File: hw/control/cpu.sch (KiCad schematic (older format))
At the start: 18 parts, among them J301 Conn_02x05_Odd_Even, J302 Conn_01x04, J303 Raspberry_Pi_0_2_3, J304 Micro_SD_Card, J305 Conn_01x06

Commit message: [hw] Assign most of the controller footprints
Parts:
- C301, C302, C303, C304, C305: footprint (none) -> Capacitor_SMD:C_0805_2012Metric_Pad1.18x1.45mm_HandSolder
- J301: footprint (none) -> Connector_PinHeader_2.54mm:PinHeader_2x05_P2.54mm_Vertical
- J302: footprint (none) -> Connector_PinHeader_2.54mm:PinHeader_1x04_P2.54mm_Vertical
- J303: footprint (none) -> Connector_PinHeader_2.54mm:PinHeader_2x20_P2.54mm_Vertical
- J305: footprint (none) -> Connector_PinHeader_2.54mm:PinHeader_1x06_P2.54mm_Vertical
- JP301, JP302: footprint (none) -> Jumper:SolderJumper-3_P1.3mm_Bridged12_RoundedPad1.0x1.5mm_NumberLabels
- R301, R302, R303, R304, R305, R306: footprint (none) -> Resistor_SMD:R_0805_2012Metric_Pad1.20x1.40mm_HandSolder
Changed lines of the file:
@@
 F 0 "J301" H 9800 1967 50  0000 C CNN
 F 1 "Conn_02x05_Odd_Even" H 9800 1876 50  0000 C CNN
-F 2 "" H 9750 1550 50  0001 C CNN
+F 2 "Connector_PinHeader_2.54mm:PinHeader_2x05_P2.54mm_Vertical" H 9750 1550 50  0001 C CNN
 F 3 "~" H 9750 1550 50  0001 C CNN
 	1    9750 1550
@@
 F 0 "R302" V 4493 2400 50  0000 C CNN
 F 1 "33R" V 4584 2400 50  0000 C CNN
-F 2 "" V 4630 2400 50  0001 C CNN
+F 2 "Resistor_SMD:R_0805_2012Metric_Pad1.20x1.40mm_HandSolder" V 4630 2400 50  0001 C CNN
 F 3 "~" H 4700 2400 50  0001 C CNN
 	1    4700 2400
@@
 F 0 "R301" V 4493 2050 50  0000 C CNN
 F 1 "33R" V 4584 2050 50  0000 C CNN
-F 2 "" V 4630 2050 50  0001 C CNN
+F 2 "Resistor_SMD:R_0805_2012Metric_Pad1.20x1.40mm_HandSolder" V 4630 2050 50  0001 C CNN
 F 3 "~" H 4700 2050 50  0001 C CNN
 	1    4700 2050
@@
 F 0 "R304" H 1430 6554 50  0000 R CNN
 F 1 "33R" H 1430 6645 50  0000 R CNN
-F 2 "" V 1430 6600 50  0001 C CNN
+F 2 "Resistor_SMD:R_0805_2012Metric_Pad1.20x1.40mm_HandSolder" V 1430 6600 50  0001 C CNN
 F 3 "~" H 1500 6600 50  0001 C CNN
 	1    1500 6600
@@
 F 0 "R305" H 1220 6846 50  0000 L CNN
 F 1 "33R" H 1220 6755 50  0000 L CNN
-F 2 "" V 1080 6800 50  0001 C CNN
+F 2 "Resistor_SMD:R_0805_2012Metric_Pad1.20x1.40mm_HandSolder" V 1080 6800 50  0001 C CNN
 F 3 "~" H 1150 6800 50  0001 C CNN
 	1    1150 6800
@@
 F 0 "C305" H 2515 5696 50  0000 L CNN
 F 1 "100n" H 2515 5605 50  0000 L CNN
-F 2 "" H 2438 5500 50  0001 C CNN
+F 2 "Capacitor_SMD:C_0805_2012Metric_Pad1.18x1.45mm_HandSolder" H 2438 5500 50  0001 C CNN
 F 3 "~" H 2400 5650 50  0001 C CNN
 	1    2400 5650
@@
 F 0 "C302" H 1515 1246 50  0000 L CNN
 F 1 "100n" H 1515 1155 50  0000 L CNN
-F 2 "" H 1438 1050 50  0001 C CNN
+F 2 "Capacitor_SMD:C_0805_2012Metric_Pad1.18x1.45mm_HandSolder" H 1438 1050 50  0001 C CNN
 F 3 "~" H 1400 1200 50  0001 C CNN
 	1    1400 1200
@@
 F 0 "C303" H 1965 1246 50  0000 L CNN
 F 1 "100n" H 1965 1155 50  0000 L CNN
-F 2 "" H 1888 1050 50  0001 C CNN
+F 2 "Capacitor_SMD:C_0805_2012Metric_Pad1.18x1.45mm_HandSolder" H 1888 1050 50  0001 C CNN
 F 3 "~" H 1850 1200 50  0001 C CNN
 	1    1850 1200
@@
 F 0 "C304" H 2415 1246 50  0000 L CNN
 F 1 "100n" H 2415 1155 50  0000 L CNN
-F 2 "" H 2338 1050 50  0001 C CNN
+F 2 "Capacitor_SMD:C_0805_2012Metric_Pad1.18x1.45mm_HandSolder" H 2338 1050 50  0001 C CNN
 F 3 "~" H 2300 1200 50  0001 C CNN
 	1    2300 1200
@@
 F 0 "C301" H 1065 1246 50  0000 L CNN
 F 1 "100n" H 1065 1155 50  0000 L CNN
-F 2 "" H 988 1050 50  0001 C CNN
+F 2 "Capacitor_SMD:C_0805_2012Metric_Pad1.18x1.45mm_HandSolder" H 988 1050 50  0001 C CNN
 F 3 "~" H 950 1200 50  0001 C CNN
 	1    950  1200
@@
 F 0 "J303" H 6900 2250 50  0000 C CNN
 F 1 "Raspberry_Pi_0_2_3" H 7200 2350 50  0000 C CNN
-F 2 "" H 6500 3650 50  0001 C CNN
+F 2 "Connector_PinHeader_2.54mm:PinHeader_2x20_P2.54mm_Vertical" H 6500 3650 50  0001 C CNN
 F 3 "https://www.raspberrypi.org/documentation/hardware/raspberrypi/schematics/rpi_SCH_3bplus_1p0_reduced.pdf" H 6500 3650 50  0001 C CNN
 	1    6500 3650
@@
 F 0 "J302" H 3568 2517 50  0000 C CNN
 F 1 "Conn_01x04" H 3568 2426 50  0000 C CNN
-F 2 "" H 3650 2200 50  0001 C CNN
+F 2 "Connector_PinHeader_2.54mm:PinHeader_1x04_P2.54mm_Vertical" H 3650 2200 50  0001 C CNN
 F 3 "~" H 3650 2200 50  0001 C CNN
 	1    3650 2200
@@
 F 0 "R303" H 1920 6546 50  0000 L CNN
 F 1 "33R" H 1920 6455 50  0000 L CNN
-F 2 "" V 1780 6500 50  0001 C CNN
+F 2 "Resistor_SMD:R_0805_2012Metric_Pad1.20x1.40mm_HandSolder" V 1780 6500 50  0001 C CNN
 F 3 "~" H 1850 6500 50  0001 C CNN
 	1    1850 6500
@@
 F 0 "R306" H 870 7046 50  0000 L CNN
 F 1 "33R" H 870 6955 50  0000 L CNN
-F 2 "" V 730 7000 50  0001 C CNN
+F 2 "Resistor_SMD:R_0805_2012Metric_Pad1.20x1.40mm_HandSolder" V 730 7000 50  0001 C CNN
 F 3 "~" H 800 7000 50  0001 C CNN
 	1    800  7000
@@
 F 0 "J305" H 5630 6692 50  0000 L CNN
 F 1 "Conn_01x06" H 5630 6601 50  0000 L CNN
-F 2 "" H 5550 6700 50  0001 C CNN
+F 2 "Connector_PinHeader_2.54mm:PinHeader_1x06_P2.54mm_Vertical" H 5550 6700 50  0001 C CNN
 F 3 "~" H 5550 6700 50  0001 C CNN
 	1    5550 6700
@@
 F 0 "JP301" H 8300 4405 50  0000 C CNN
 F 1 "Jumper" H 8300 4314 50  0000 C CNN
-F 2 "" H 8300 4200 50  0001 C CNN
+F 2 "Jumper:SolderJumper-3_P1.3mm_Bridged12_RoundedPad1.0x1.5mm_NumberLabels" H 8300 4200 50  0001 C CNN
 F 3 "~" H 8300 4200 50  0001 C CNN
 	1    8300 4200
@@
 F 0 "JP302" H 8000 4805 50  0000 C CNN
 F 1 "Jumper" H 8000 4714 50  0000 C CNN
-F 2 "" H 8000 4600 50  0001 C CNN
+F 2 "Jumper:SolderJumper-3_P1.3mm_Bridged12_RoundedPad1.0x1.5mm_NumberLabels" H 8000 4600 50  0001 C CNN
 F 3 "~" H 8000 4600 50  0001 C CNN
 	1    8000 4600

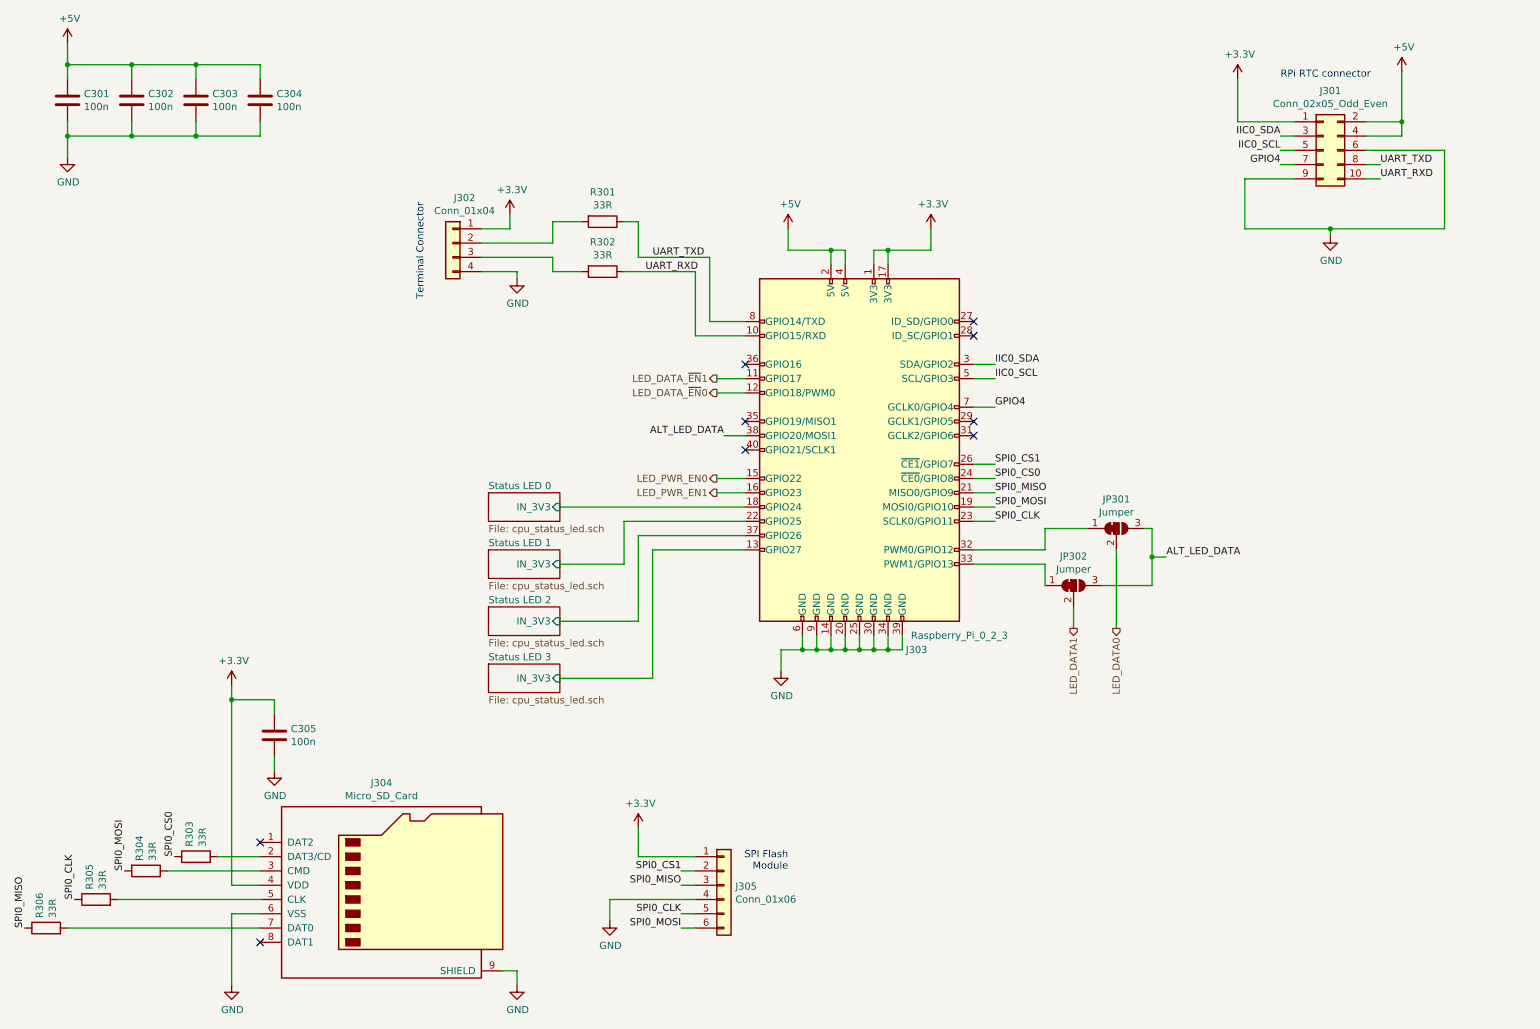
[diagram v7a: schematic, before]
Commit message: [hw] Assign control board footprints
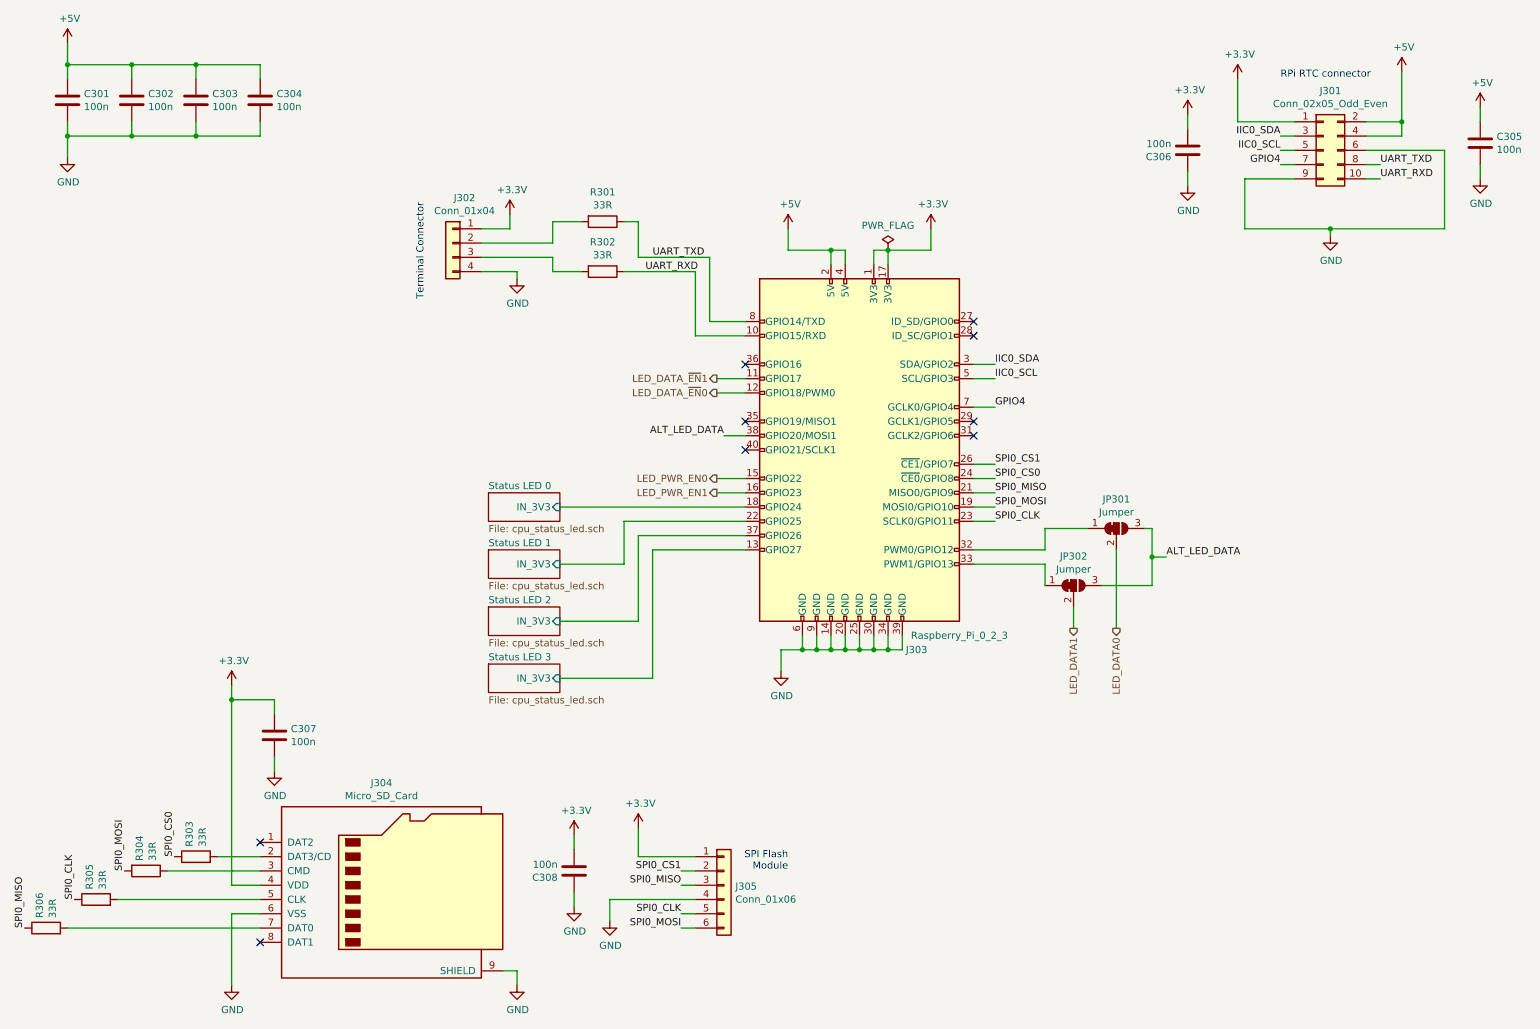
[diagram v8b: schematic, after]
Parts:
- added C305, C306, C308: 100n, Capacitor_SMD:C_0805_2012Metric_Pad1.18x1.45mm_HandSolder, symbol Device:C
- renumbered C305 to C307
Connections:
- net +3V3: now also C306.2, C308.2
- net +5V: now also C305.1
- net GND: now also C305.2, C306.1, C308.1
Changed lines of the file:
@@
 P 5950 5200
 AR Path="/614A2C71" Ref="#PWR?"  Part="1"
-AR Path="/6148E1AC/614A2C71" Ref="#PWR0310"  Part="1"
-F 0 "#PWR0310" H 5950 4950 50  0001 C CNN
+AR Path="/6148E1AC/614A2C71" Ref="#PWR0314"  Part="1"
+F 0 "#PWR0314" H 5950 4950 50  0001 C CNN
 F 1 "GND" H 5955 5027 50  0000 C CNN
 F 2 "" H 5950 5200 50  0001 C CNN
@@
 P 6000 2100
 AR Path="/614A2C87" Ref="#PWR?"  Part="1"
-AR Path="/6148E1AC/614A2C87" Ref="#PWR0306"  Part="1"
-F 0 "#PWR0306" H 6000 1950 50  0001 C CNN
+AR Path="/6148E1AC/614A2C87" Ref="#PWR0310"  Part="1"
+F 0 "#PWR0310" H 6000 1950 50  0001 C CNN
 F 1 "+5V" H 6015 2273 50  0000 C CNN
 F 2 "" H 6000 2100 50  0001 C CNN
@@
 P 7000 2100
 AR Path="/614A2C91" Ref="#PWR?"  Part="1"
-AR Path="/6148E1AC/614A2C91" Ref="#PWR0307"  Part="1"
-F 0 "#PWR0307" H 7000 1950 50  0001 C CNN
+AR Path="/6148E1AC/614A2C91" Ref="#PWR0311"  Part="1"
+F 0 "#PWR0311" H 7000 1950 50  0001 C CNN
 F 1 "+3.3V" H 7015 2273 50  0000 C CNN
 F 2 "" H 7000 2100 50  0001 C CNN
@@
 P 9800 2150
 AR Path="/614A2CB4" Ref="#PWR?"  Part="1"
-AR Path="/6148E1AC/614A2CB4" Ref="#PWR0308"  Part="1"
-F 0 "#PWR0308" H 9800 1900 50  0001 C CNN
+AR Path="/6148E1AC/614A2CB4" Ref="#PWR0312"  Part="1"
+F 0 "#PWR0312" H 9800 1900 50  0001 C CNN
 F 1 "GND" H 9805 1977 50  0000 C CNN
 F 2 "" H 9800 2150 50  0001 C CNN
@@
 	1    0    0    -1
 $EndComp
-Wire Wire Line
-	10600 2100 10600 1550
 Wire Wire Line
 	10600 1550 10050 1550
@@
 LED_PWR_EN1
 $Comp
-L power:GND #PWR0309
+L power:GND #PWR0313
 U 1 1 6146B045
 P 4100 2450
-F 0 "#PWR0309" H 4100 2200 50  0001 C CNN
+F 0 "#PWR0313" H 4100 2200 50  0001 C CNN
 F 1 "GND" H 4105 2277 50  0000 C CNN
 F 2 "" H 4100 2450 50  0001 C CNN
@@
 	7300 4050 7450 4050
 $Comp
-L power:+3.3V #PWR0311
+L power:+3.3V #PWR0315
 U 1 1 614C61E8
 P 2100 5300
-F 0 "#PWR0311" H 2100 5150 50  0001 C CNN
+F 0 "#PWR0315" H 2100 5150 50  0001 C CNN
 F 1 "+3.3V" H 2115 5473 50  0000 C CNN
 F 2 "" H 2100 5300 50  0001 C CNN
@@
 $EndComp
 $Comp
-L Device:C C305
+L Device:C C307
 U 1 1 614C7B6C
 P 2400 5650
-F 0 "C305" H 2515 5696 50  0000 L CNN
+F 0 "C307" H 2515 5696 50  0000 L CNN
 F 1 "100n" H 2515 5605 50  0000 L CNN
 F 2 "Capacitor_SMD:C_0805_2012Metric_Pad1.18x1.45mm_HandSolder" H 2438 5500 50  0001 C CNN
@@
 $EndComp
 $Comp
-L power:GND #PWR0312
+L power:GND #PWR0316
 U 1 1 614CAAF2
 P 2400 5900
-F 0 "#PWR0312" H 2400 5650 50  0001 C CNN
+F 0 "#PWR0316" H 2400 5650 50  0001 C CNN
 F 1 "GND" H 2405 5727 50  0000 C CNN
 F 2 "" H 2400 5900 50  0001 C CNN
@@
 	2100 6700 2300 6700
 $Comp
-L power:GND #PWR0315
+L power:GND #PWR0321
 U 1 1 614D028A
 P 2100 7400
-F 0 "#PWR0315" H 2100 7150 50  0001 C CNN
+F 0 "#PWR0321" H 2100 7150 50  0001 C CNN
 F 1 "GND" H 2105 7227 50  0000 C CNN
 F 2 "" H 2100 7400 50  0001 C CNN
@@
 	2100 6900 2100 7400
 $Comp
-L power:GND #PWR0316
+L power:GND #PWR0322
 U 1 1 614D2941
 P 4100 7400
-F 0 "#PWR0316" H 4100 7150 50  0001 C CNN
+F 0 "#PWR0322" H 4100 7150 50  0001 C CNN
 F 1 "GND" H 4105 7227 50  0000 C CNN
 F 2 "" H 4100 7400 50  0001 C CNN
@@
 $EndComp
 $Comp
-L power:GND #PWR0304
+L power:GND #PWR0306
 U 1 1 61474A2C
 P 950 1600
-F 0 "#PWR0304" H 950 1350 50  0001 C CNN
+F 0 "#PWR0306" H 950 1350 50  0001 C CNN
 F 1 "GND" H 955 1427 50  0000 C CNN
 F 2 "" H 950 1600 50  0001 C CNN
@@
 NoConn ~ 2300 7100
 $Comp
-L power:+3.3V #PWR0313
+L power:+3.3V #PWR0317
 U 1 1 6164D788
 P 4950 6300
-F 0 "#PWR0313" H 4950 6150 50  0001 C CNN
+F 0 "#PWR0317" H 4950 6150 50  0001 C CNN
 F 1 "+3.3V" H 4965 6473 50  0000 C CNN
 F 2 "" H 4950 6300 50  0001 C CNN
@@
 	4950 6500 5350 6500
 $Comp
-L power:GND #PWR0314
+L power:GND #PWR0320
 U 1 1 6166C611
 P 4750 6950
-F 0 "#PWR0314" H 4750 6700 50  0001 C CNN
+F 0 "#PWR0320" H 4750 6700 50  0001 C CNN
 F 1 "GND" H 4755 6777 50  0000 C CNN
 F 2 "" H 4750 6950 50  0001 C CNN
@@
 $EndComp
 $Comp
-L power:+3.3V #PWR0305
+L power:+3.3V #PWR0309
 U 1 1 61801CAF
 P 4050 2000
-F 0 "#PWR0305" H 4050 1850 50  0001 C CNN
+F 0 "#PWR0309" H 4050 1850 50  0001 C CNN
 F 1 "+3.3V" H 4065 2173 50  0000 C CNN
 F 2 "" H 4050 2000 50  0001 C CNN
@@
 Text Notes 3450 2600 1    50   ~ 0
 Terminal Connector
+$Comp
+L power:PWR_FLAG #FLG0301
+U 1 1 61666440
+P 6700 2250
+F 0 "#FLG0301" H 6700 2325 50  0001 C CNN
+F 1 "PWR_FLAG" H 6700 2423 50  0000 C CNN
+F 2 "" H 6700 2250 50  0001 C CNN
+F 3 "~" H 6700 2250 50  0001 C CNN
+	1    6700 2250
+	1    0    0    -1
+$EndComp
+$Comp
+L Device:C C308
+U 1 1 61666109
+P 4500 6600
+F 0 "C308" H 4615 6646 50  0000 L CNN
+F 1 "100n" H 4615 6555 50  0000 L CNN
+F 2 "Capacitor_SMD:C_0805_2012Metric_Pad1.18x1.45mm_HandSolder" H 4538 6450 50  0001 C CNN
+F 3 "~" H 4500 6600 50  0001 C CNN
+	1    4500 6600
+	-1   0    0    1
+$EndComp
+$Comp
+L Device:C C306
+U 1 1 6166B8E9
+P 8800 1550
+F 0 "C306" H 8915 1596 50  0000 L CNN
+F 1 "100n" H 8915 1505 50  0000 L CNN
+F 2 "Capacitor_SMD:C_0805_2012Metric_Pad1.18x1.45mm_HandSolder" H 8838 1400 50  0001 C CNN
+F 3 "~" H 8800 1550 50  0001 C CNN
+	1    8800 1550
+	-1   0    0    1
+$EndComp
+$Comp
+L Device:C C305
+U 1 1 61671F8B
+P 10850 1500
+F 0 "C305" H 10965 1546 50  0000 L CNN
+F 1 "100n" H 10965 1455 50  0000 L CNN
+F 2 "Capacitor_SMD:C_0805_2012Metric_Pad1.18x1.45mm_HandSolder" H 10888 1350 50  0001 C CNN
+F 3 "~" H 10850 1500 50  0001 C CNN
+	1    10850 1500
+	1    0    0    -1
+$EndComp
+Wire Wire Line
+	8800 1400 8800 1300
+Wire Wire Line
+	8800 1700 8800 1800
+$Comp
+L power:GND #PWR0319
+U 1 1 6168F7F5
+P 4500 6850
+F 0 "#PWR0319" H 4500 6600 50  0001 C CNN
+F 1 "GND" H 4505 6677 50  0000 C CNN
+F 2 "" H 4500 6850 50  0001 C CNN
+F 3 "" H 4500 6850 50  0001 C CNN
+	1    4500 6850
+	1    0    0    -1
+$EndComp
+$Comp
+L power:+3.3V #PWR0318
+U 1 1 6169033D
+P 4500 6350
+F 0 "#PWR0318" H 4500 6200 50  0001 C CNN
+F 1 "+3.3V" H 4515 6523 50  0000 C CNN
+F 2 "" H 4500 6350 50  0001 C CNN
+F 3 "" H 4500 6350 50  0001 C CNN
+	1    4500 6350
+	1    0    0    -1
+$EndComp
+Wire Wire Line
+	4500 6350 4500 6450
+Wire Wire Line
+	4500 6750 4500 6850
+$Comp
+L power:+3.3V #PWR0305
+U 1 1 616B37CF
+P 8800 1300
+F 0 "#PWR0305" H 8800 1150 50  0001 C CNN
+F 1 "+3.3V" H 8815 1473 50  0000 C CNN
+F 2 "" H 8800 1300 50  0001 C CNN
+F 3 "" H 8800 1300 50  0001 C CNN
+	1    8800 1300
+	1    0    0    -1
+$EndComp
+$Comp
+L power:GND #PWR0308
+U 1 1 616B9C8D
+P 8800 1800
+F 0 "#PWR0308" H 8800 1550 50  0001 C CNN
+F 1 "GND" H 8805 1627 50  0000 C CNN
+F 2 "" H 8800 1800 50  0001 C CNN
+F 3 "" H 8800 1800 50  0001 C CNN
+	1    8800 1800
+	1    0    0    -1
+$EndComp
+Wire Wire Line
+	10600 1550 10600 2100
+$Comp
+L power:GND #PWR0307
+U 1 1 616BFE51
+P 10850 1750
+F 0 "#PWR0307" H 10850 1500 50  0001 C CNN
+F 1 "GND" H 10855 1577 50  0000 C CNN
+F 2 "" H 10850 1750 50  0001 C CNN
+F 3 "" H 10850 1750 50  0001 C CNN
+	1    10850 1750
+	1    0    0    -1
+$EndComp
+Wire Wire Line
+	10850 1750 10850 1650
+$Comp
+L power:+5V #PWR0304
+U 1 1 616C6A93
+P 10850 1250
+F 0 "#PWR0304" H 10850 1100 50  0001 C CNN
+F 1 "+5V" H 10865 1423 50  0000 C CNN
+F 2 "" H 10850 1250 50  0001 C CNN
+F 3 "" H 10850 1250 50  0001 C CNN
+	1    10850 1250
+	1    0    0    -1
+$EndComp
+Wire Wire Line
+	10850 1250 10850 1350
 $EndSCHEMATC
